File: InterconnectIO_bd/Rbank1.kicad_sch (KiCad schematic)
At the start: 48 parts, among them K1 TQ2-5, K2 TQ2-5, K3 TQ2-5, K4 TQ2-5, K5 TQ2-5, K6 TQ2-5, K7 TQ2-5, K8 TQ2-5, K9 TQ2-5

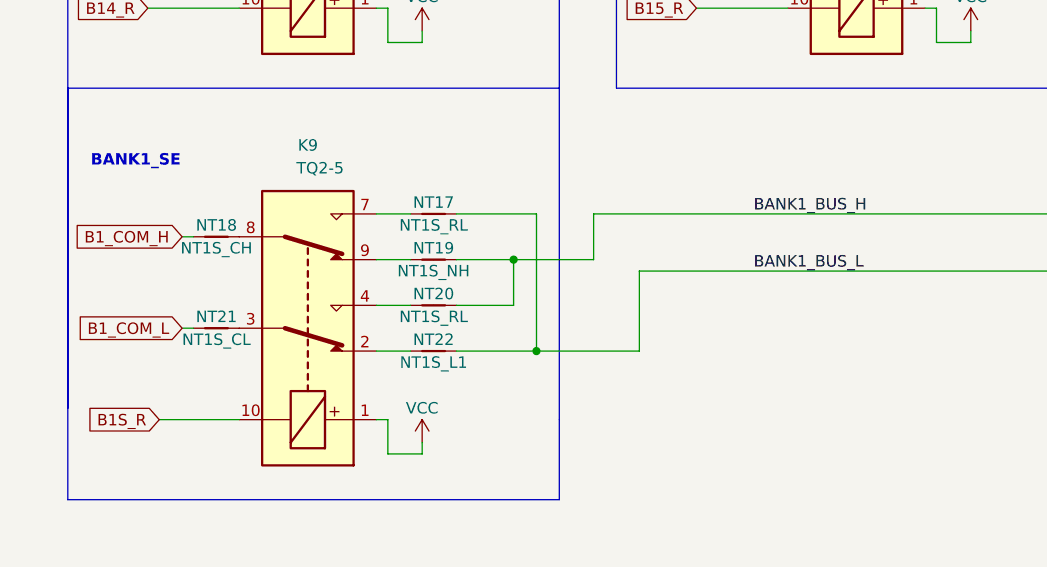
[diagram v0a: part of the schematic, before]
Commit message: Reverse COM_H and COM_L on relay Bank
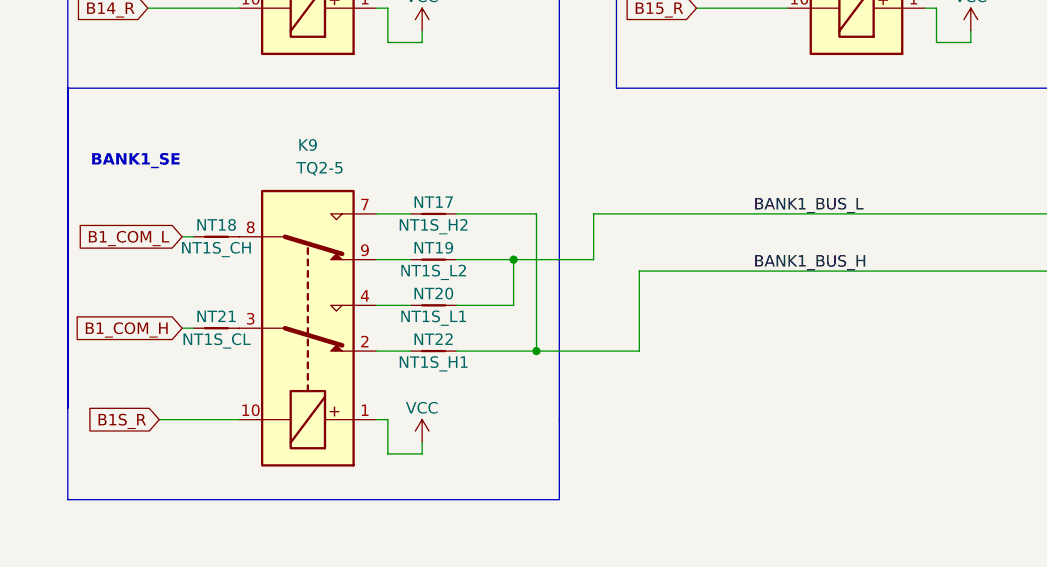
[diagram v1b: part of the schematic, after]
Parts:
- NT17: value NT1S_RL -> NT1S_H2
- NT19: value NT1S_NH -> NT1S_L2
- NT20: value NT1S_RL -> NT1S_L1
- NT22: value NT1S_L1 -> NT1S_H1
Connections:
- net B1_COM_H: now also NT21.1; no longer NT18.1
- net B1_COM_L: now also NT18.1; no longer NT21.1
- net BANK1_BUS_H: now also NT1.1, NT10.1, NT11.1, NT12.1, NT17.2, NT2.1, NT22.2, NT3.1, NT4.1, NT9.1; no longer NT13.1, NT14.1, NT15.1, NT16.1, NT19.2, NT20.2, NT5.1, NT6.1, NT7.1, NT8.1
- net BANK1_BUS_L: now also NT13.1, NT14.1, NT15.1, NT16.1, NT19.2, NT20.2, NT5.1, NT6.1, NT7.1, NT8.1; no longer NT1.1, NT10.1, NT11.1, NT12.1, NT17.2, NT2.1, NT22.2, NT3.1, NT4.1, NT9.1
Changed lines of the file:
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@@
     (effects (font (size 1.27 1.27)) (justify left bottom))
   )
-  (label "BANK1_BUS_L" (at 97.79 129.54 0) (fields_autoplaced)
+  (label "BANK1_BUS_H" (at 97.79 129.54 0) (fields_autoplaced)
     (effects (font (size 1.27 1.27)) (justify left bottom))
   )
@@
     (effects (font (size 1.27 1.27)) (justify left bottom))
   )
-  (label "BANK1_BUS_H" (at 97.79 123.19 0) (fields_autoplaced)
+  (label "BANK1_BUS_L" (at 97.79 123.19 0) (fields_autoplaced)
     (effects (font (size 1.27 1.27)) (justify left bottom))
   )
@@
     )
   )
-  (global_label "B1_COM_H" (shape input) (at 34.29 125.73 180) (fields_autoplaced)
+  (global_label "B1_COM_L" (shape input) (at 34.29 125.73 180) (fields_autoplaced)
     (effects (font (size 1.27 1.27)) (justify right))
-    (property "Intersheetrefs" "${INTERSHEET_REFS}" (at 22.0798 125.6506 0)
+    (property "Intersheetrefs" "${INTERSHEET_REFS}" (at 21.8895 125.73 0)
       (effects (font (size 1.27 1.27)) (justify right) hide)
     )
@@
     )
   )
-  (global_label "B1_COM_L" (shape input) (at 34.29 135.89 180) (fields_autoplaced)
+  (global_label "B1_COM_H" (shape input) (at 34.29 135.89 180) (fields_autoplaced)
     (effects (font (size 1.27 1.27)) (justify right))
-    (property "Intersheetrefs" "${INTERSHEET_REFS}" (at 22.3821 135.8106 0)
+    (property "Intersheetrefs" "${INTERSHEET_REFS}" (at 21.5871 135.89 0)
       (effects (font (size 1.27 1.27)) (justify right) hide)
     )
@@
       (effects (font (size 1.27 1.27)))
     )
-    (property "Value" "NT1S_RL" (at 62.23 124.46 0)
+    (property "Value" "NT1S_H2" (at 62.23 124.46 0)
       (effects (font (size 1.27 1.27)))
     )
@@
       (effects (font (size 1.27 1.27)))
     )
-    (property "Value" "NT1S_L1" (at 62.23 139.7 0)
+    (property "Value" "NT1S_H1" (at 62.23 139.7 0)
       (effects (font (size 1.27 1.27)))
     )
@@
       (effects (font (size 1.27 1.27)))
     )
-    (property "Value" "NT1S_NH" (at 62.23 129.54 0)
+    (property "Value" "NT1S_L2" (at 62.23 129.54 0)
       (effects (font (size 1.27 1.27)))
     )
@@
       (effects (font (size 1.27 1.27)))
     )
-    (property "Value" "NT1S_RL" (at 62.23 134.62 0)
-      (effects (font (size 1.27 1.27)))
-    )
+    (property "Value" "NT1S_L1" (at 62.23 134.62 0)
+      (effects (font (size 1.27 1.27)))
+    )
